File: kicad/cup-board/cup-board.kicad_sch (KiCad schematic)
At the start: 29 parts, among them J2 EARCUP_SPKR, J3 CUP_PWR_IN, J4 VLED_IN, J5 AIRCRAFT_AUDIO_IN, J6 RLY_COIL_IN, K1 G6K-2F-Y DC5, T1 SP-74, U1 ADAU1861, U2 LSM6DSV16BX, U3 MAXM86161

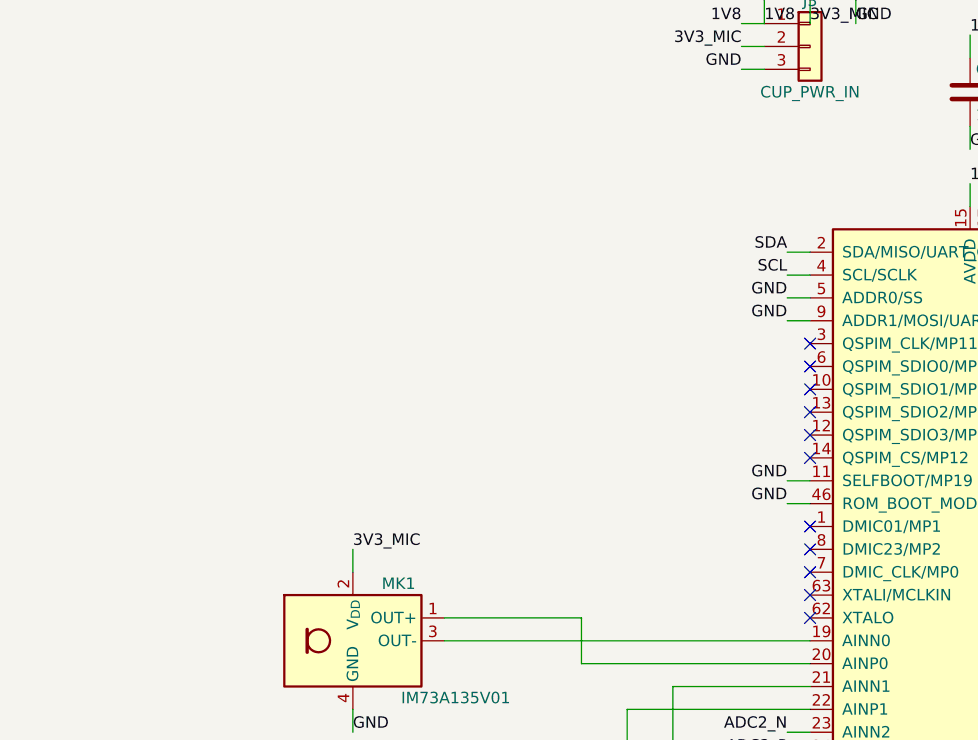
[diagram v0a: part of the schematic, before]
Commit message: [LIMA] cup-board: add IM72D128V PDM voice mic (MK3) on U1 DMIC01, per Peter
One IM72D128V for voice pickup on U1's digital-mic port, so ADC0/1 (ANC mics) and
ADC2 (aircraft audio) are untouched. Wiring copies the audio board (4f1c7a8):
DATA -> DMIC_DATA -> DMIC01/MP1, CLOCK <- DMIC_CLK <- DMIC_CLK/MP0, VDD on 1V8
with C11 1uF bypass, LR -> GND (DATA1, falling edge). DMIC23 stays no-connect.
The pre-existing no-connect flags on DMIC01 and DMIC_CLK are removed. Infineon
symbol library registered in the project sym-lib-table.

Verified: netlist adds only DMIC_DATA = MK3.1, U1.1; DMIC_CLK = MK3.3, U1.7;
MK3/C11 on 1V8 and GND. ERC 0 errors, same 8 pre-existing warnings;
find_shorted_nets 0; overlaps 0. SVG re-exported; README updated.

Co-Authored-By: Claude Opus 5.5 <noreply@anthropic.com>
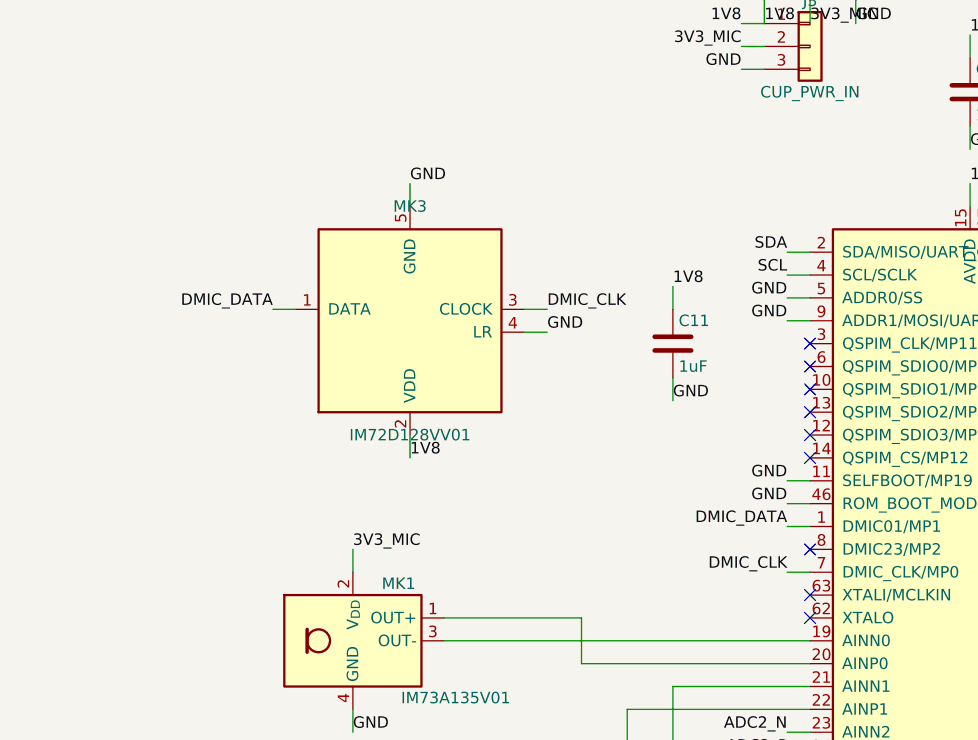
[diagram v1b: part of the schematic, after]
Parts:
- added C11: 1uF, symbol Device:C
- added MK3: IM72D128VV01, symbol Infineon:IM72D128V
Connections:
- net 1V8: now also C11.1, MK3.2 (VDD)
- net GND: now also C11.2, MK3.4 (LR), MK3.5 (GND)
- net DMIC_DATA: now reaches U1.1 (DMIC01/MP1)
- net DMIC_DATA: now also MK3.1 (DATA)
- net DMIC_CLK: now reaches U1.7 (DMIC_CLK/MP0)
- net DMIC_CLK: now also MK3.3 (CLOCK)
- no-connect marks 36 -> 34
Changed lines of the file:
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@@
 	)
 	(no_connect
-		(at 165.1 138.43)
-	)
-	(no_connect
-		(at 165.1 140.97)
-	)
-	(no_connect
-		(at 165.1 143.51)
-	)
-	(no_connect
 		(at 165.1 146.05)
 	)
@@
 		(at 314.96 231.14)
 	)
+	(no_connect
+		(at 165.1 140.97)
+	)
 	(wire
 		(pts
@@
 		)
 	)
+	(wire
+		(pts
+			(xy 107.95 114.3)
+			(xy 105.41 114.3)
+		)
+	)
+	(wire
+		(pts
+			(xy 120.65 128.27)
+			(xy 120.65 130.81)
+		)
+	)
+	(wire
+		(pts
+			(xy 133.35 114.3)
+			(xy 135.89 114.3)
+		)
+	)
+	(wire
+		(pts
+			(xy 133.35 116.84)
+			(xy 135.89 116.84)
+		)
+	)
+	(wire
+		(pts
+			(xy 120.65 102.87)
+			(xy 120.65 100.33)
+		)
+	)
+	(wire
+		(pts
+			(xy 165.1 138.43)
+			(xy 162.56 138.43)
+		)
+	)
+	(wire
+		(pts
+			(xy 165.1 143.51)
+			(xy 162.56 143.51)
+		)
+	)
+	(wire
+		(pts
+			(xy 149.86 114.3)
+			(xy 149.86 111.76)
+		)
+	)
+	(wire
+		(pts
+			(xy 149.86 121.92)
+			(xy 149.86 124.46)
+		)
+	)
 	(label "1V8"
 		(at 160.02 82.55 0)
@@
 		)
 	)
+	(label "DMIC_DATA"
+		(at 105.41 114.3 180)
+		(effects
+			(font
+				(size 1.27 1.27)
+			)
+			(justify right bottom)
+		)
+	)
+	(label "1V8"
+		(at 120.65 130.81 0)
+		(effects
+			(font
+				(size 1.27 1.27)
+			)
+			(justify left bottom)
+		)
+	)
+	(label "DMIC_CLK"
+		(at 135.89 114.3 0)
+		(effects
+			(font
+				(size 1.27 1.27)
+			)
+			(justify left bottom)
+		)
+	)
+	(label "GND"
+		(at 135.89 116.84 0)
+		(effects
+			(font
+				(size 1.27 1.27)
+			)
+			(justify left bottom)
+		)
+	)
+	(label "GND"
+		(at 120.65 100.33 0)
+		(effects
+			(font
+				(size 1.27 1.27)
+			)
+			(justify left bottom)
+		)
+	)
+	(label "DMIC_DATA"
+		(at 162.56 138.43 180)
+		(effects
+			(font
+				(size 1.27 1.27)
+			)
+			(justify right bottom)
+		)
+	)
+	(label "DMIC_CLK"
+		(at 162.56 143.51 180)
+		(effects
+			(font
+				(size 1.27 1.27)
+			)
+			(justify right bottom)
+		)
+	)
+	(label "1V8"
+		(at 149.86 111.76 0)
+		(effects
+			(font
+				(size 1.27 1.27)
+			)
+			(justify left bottom)
+		)
+	)
+	(label "GND"
+		(at 149.86 124.46 0)
+		(effects
+			(font
+				(size 1.27 1.27)
+			)
+			(justify left bottom)
+		)
+	)
 	(symbol
 		(lib_id "AnalogDevices:ADAU1861")
@@
 					(unit 1)
 				)
+			)
+		)
+	)
+	(symbol
+		(lib_id "Infineon:IM72D128V")
+		(at 120.65 115.57 0)
+		(unit 1)
+		(in_bom yes)
+		(on_board yes)
+		(dnp no)
+		(property "Reference" "MK3"
+			(at 120.65 102.87 0)
+			(effects
+				(font
+					(size 1.27 1.27)
+				)
+			)
+		)
+		(property "Value" "IM72D128VV01"
+			(at 120.65 128.27 0)
+			(effects
+				(font
+					(size 1.27 1.27)
+				)
+			)
+		)
+		(property "Footprint" ""
+			(at 120.65 115.57 0)
+			(hide yes)
+			(effects
+				(font
+					(size 1.27 1.27)
+				)
+			)
+		)
+		(property "Datasheet" ""
+			(at 120.65 115.57 0)
+			(hide yes)
+			(effects
+				(font
+					(size 1.27 1.27)
+				)
+			)
+		)
+		(instances
+			(project "cup-board"
+				(path "/790ac8fa-b8c8-432b-bc66-3eedd04170ff"
+					(reference "MK3")
+					(unit 1)
+				)
+			)
+		)
+	)
+	(symbol
+		(lib_id "Device:C")
+		(at 149.86 118.11 0)
+		(unit 1)
+		(in_bom yes)
+		(on_board yes)
+		(dnp no)
+		(property "Reference" "C11"
+			(at 150.495 115.57 0)
+			(effects
+				(font
+					(size 1.27 1.27)
+				)
+				(justify left)
+			)
+		)
+		(property "Value" "1uF"
+			(at 150.495 120.65 0)
+			(effects
+				(font
+					(size 1.27 1.27)
+				)
+				(justify left)
+			)
+		)
+		(property "Footprint" ""
+			(at 149.86 118.11 0)
+			(hide yes)
+			(effects
+				(font
+					(size 1.27 1.27)
+				)
+			)
+		)
+		(property "Datasheet" ""
+			(at 149.86 118.11 0)
+			(hide yes)
+			(effects
+				(font
+					(size 1.27 1.27)
+				)
+			)
+		)
+		(instances
+			(project "cup-board"
+				(path "/790ac8fa-b8c8-432b-bc66-3eedd04170ff"
+					(reference "C11")
+					(unit 1)
+				)

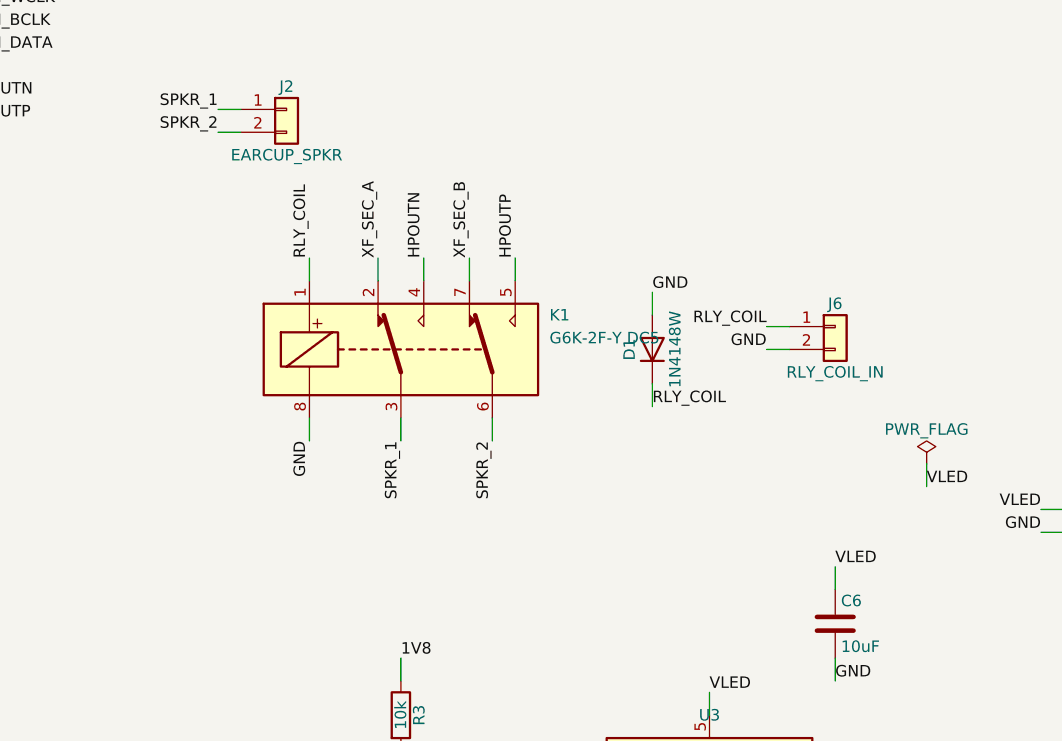
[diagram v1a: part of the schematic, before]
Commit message: [LIMA] cup-board: replace relay K1 with an AQW612S PhotoMOS pair (U4/U5), per Peter
Fail-passive speaker switch without contacts. One AQW612S (1 Form A + 1 Form B) per
speaker leg, keeping K1's pairing: U4 SPKR_1 <- XF_SEC_A (N.C.) / HPOUTN (N.O.);
U5 SPKR_2 <- XF_SEC_B (N.C.) / HPOUTP (N.O.). N.C. is closed at IF = 0, so an
unpowered cup still plays panel audio through T1. LEDs in series per part (pins 2-3
linked) from SW_DRV via 330R (R7/R8): ~8 mA typ, >=5.3 mA worst case at 5 V +/-5%.
D1 (coil flyback) removed; J6 net RLY_COIL renamed SW_DRV.

New symbol Panasonic:AQW612S in kicad/lib/Panasonic.kicad_sym, drawn from the
datasheet's p. 6 schematic (ASCTB137E 202601); library registered in the project.

Verified: netlist diff is exactly K1/D1 out, U4/U5/R7/R8 in, RLY_COIL -> SW_DRV.
ERC 0 errors, same 8 pre-existing warnings; find_shorted_nets 0; overlaps 0;
render checked. README: new "Speaker switch" section with open items (THD
unspecified, ~82 mW drive, firmware HP mute >=5 ms at power-up).

Co-Authored-By: Claude Opus 5.5 <noreply@anthropic.com>
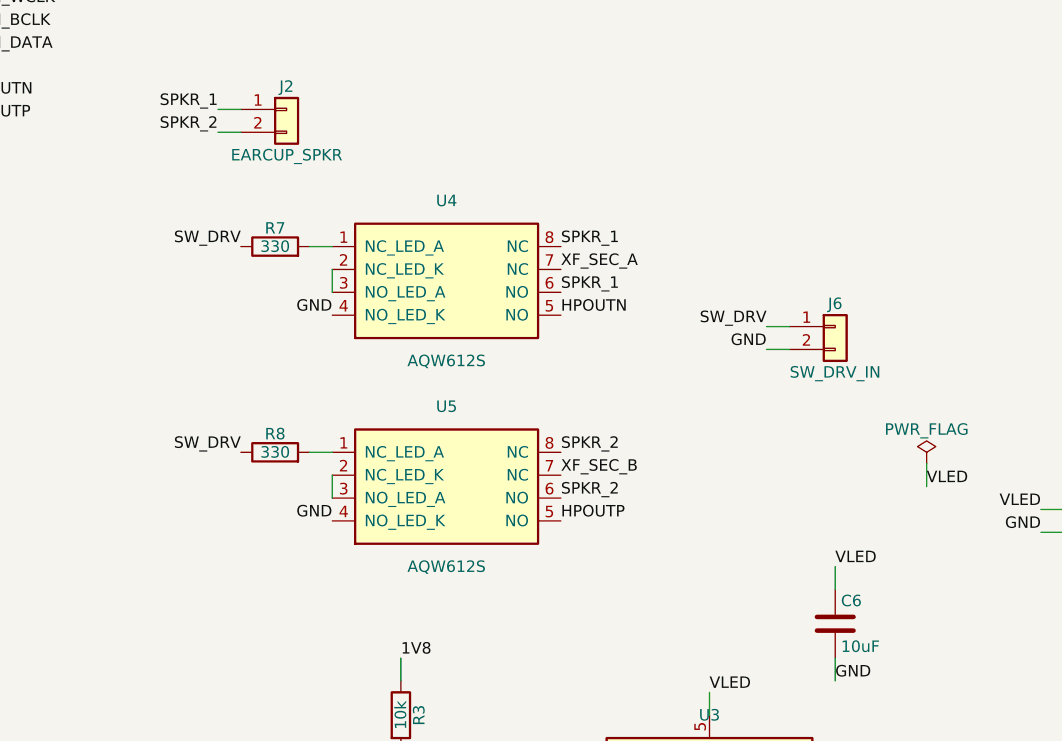
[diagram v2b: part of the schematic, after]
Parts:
- removed D1: 1N4148W, symbol Device:D
- removed K1: G6K-2F-Y DC5, symbol Relay:G6K-2
- added R7, R8: 330, symbol Device:R
- added U4, U5: AQW612S, symbol Panasonic:AQW612S
- J6: value RLY_COIL_IN -> SW_DRV_IN
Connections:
- net GND: now also U4.4 (NO_LED_K), U5.4 (NO_LED_K)
- net HPOUTN: now also U4.5 (NO)
- net HPOUTP: now also U5.5 (NO)
- net SPKR_1: now also U4.6 (NO), U4.8 (NC)
- net SPKR_2: now also U5.6 (NO), U5.8 (NC)
- net XF_SEC_A: now also U4.7 (NC)
- net XF_SEC_B: now also U5.7 (NC)
- net RLY_COIL renamed SW_DRV
- net SW_DRV: now also R7.1, R8.1
- new net: R8.2, U5.1 (NC_LED_A)
- new net: U5.2 (NC_LED_K), U5.3 (NO_LED_A)
- new net: R7.2, U4.1 (NC_LED_A)
- new net: U4.2 (NC_LED_K), U4.3 (NO_LED_A)

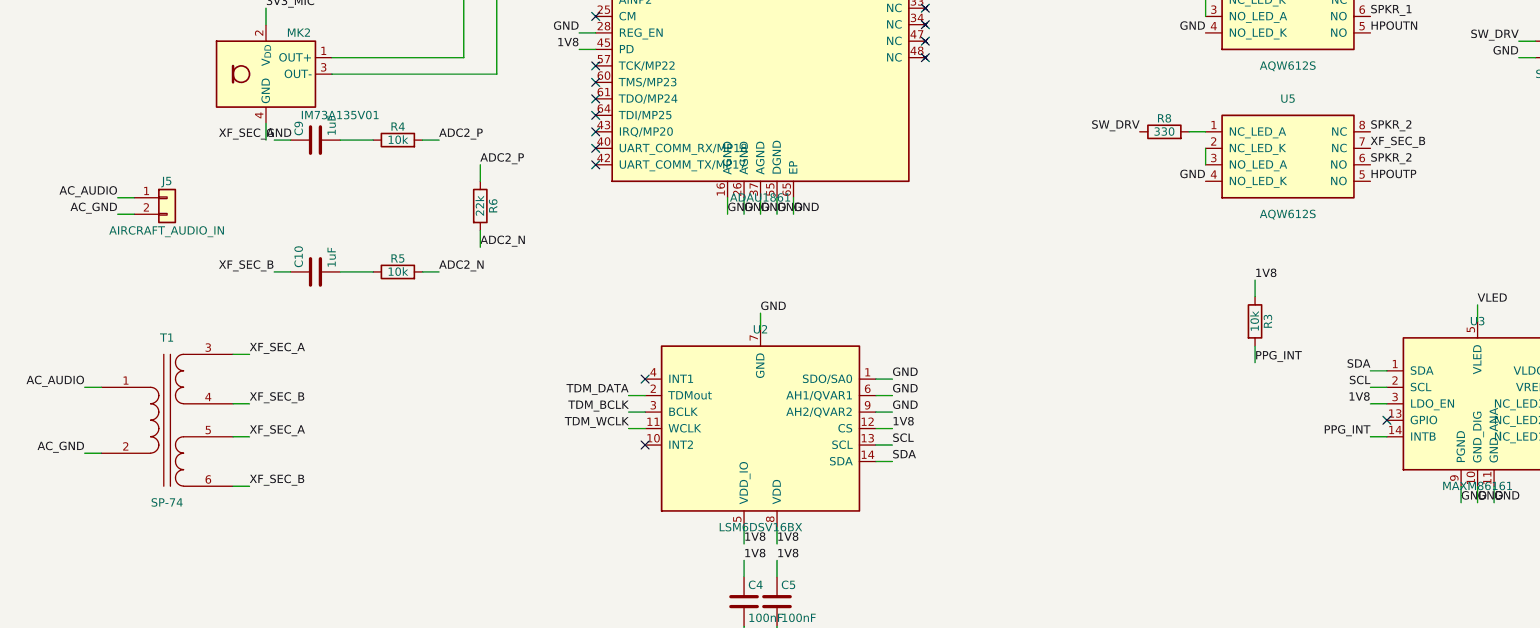
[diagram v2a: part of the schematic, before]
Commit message: [LIMA] audio board: SP-74 per cup + AQW612S mic backup; cup T1 moved off, per Peter
Audio board, AIRCRAFT AUDIO I/O sheet:
- TX: relay K1 (+D1) replaced by AQW612S U12. N.C. = boom mic (J4.1) to
  aircraft Tip, so the pilot can still transmit unpowered; the aircraft's mic
  bias still flows DC-direct through it. N.O. = the existing T1/R13 injection
  path. Drive: 4.5 V (U11) -> R15 220R -> both LEDs in series -> Q1 low side
  (kept, with R10 pulldown): ~10 mA typ, >=6 mA worst case.
- RX: mute relay K2 (+Q2/D3/R14) removed. Two SP-74s (T2 left, T3 right),
  primaries in parallel on Ring/Sleeve, secondaries to J6/J7 for each cup.
  One per cup so a shorted cable can't silence both cups. GPIO_RLY_RX_MUTE_3V3
  removed (sheet pin, labels); J1 pin 8 spare, no-connect.
- Orphan no-connects and junctions from the relays removed; sheet notes
  rewritten (relay history: commits 6e258c8..e763f7c).

Cup board: T1 removed; J5 now receives the isolated secondary pair as
XF_SEC_A/XF_SEC_B (feeds U4/U5 N.C. and the ADC2 tap, unchanged).

Verified: audio-board ERC 45 errors (= baseline, all pre-existing main-sheet
unconnected pins), warnings 12 -> 11; netlist diff exactly as intended;
find_shorted_nets 0, overlaps 0, sheet pins valid; rendered. Cup board: ERC 0
errors / same 8 warnings, netlist diff exactly T1 out and J5 relabelled.
Note: kicad-cli did not register two plain pin-to-pin wires (R15-U12.1,
U12.2-U12.3) although their endpoints matched the pins exactly; replaced with
net labels (TX_SW_A, TX_SW_MID), after which all pins appear. Root cause not found.

Co-Authored-By: Claude Opus 5.5 <noreply@anthropic.com>
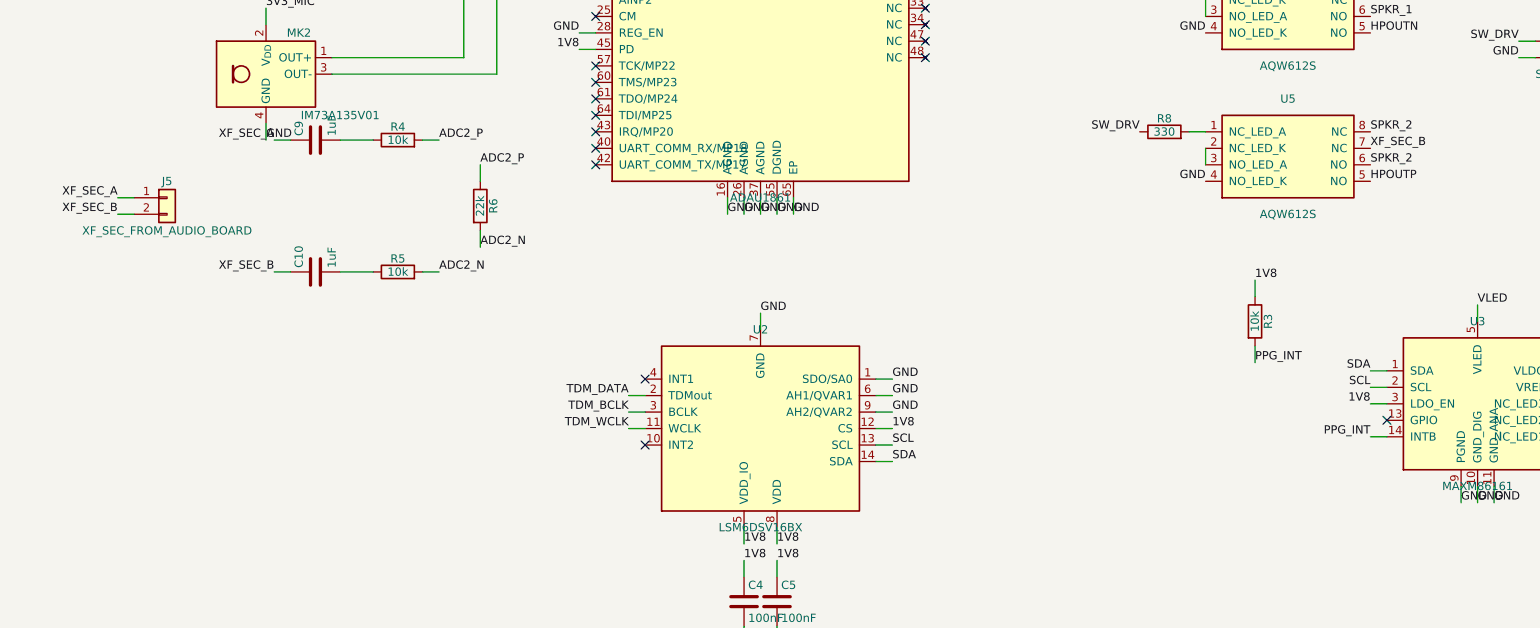
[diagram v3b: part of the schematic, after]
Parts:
- removed T1: SP-74, symbol Device:Transformer_1P_2S
- J5: value AIRCRAFT_AUDIO_IN -> XF_SEC_FROM_AUDIO_BOARD
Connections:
- net AC_AUDIO is gone; now on net XF_SEC_A: J5.1 (Pin_1)
- net AC_GND is gone; now on net XF_SEC_B: J5.2 (Pin_2)
